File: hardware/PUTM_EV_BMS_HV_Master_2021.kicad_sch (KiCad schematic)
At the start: 22 parts, among them SW1 RESET, U19 STM32F446RETx, Y1 20MHz, Y2 32.768kHz

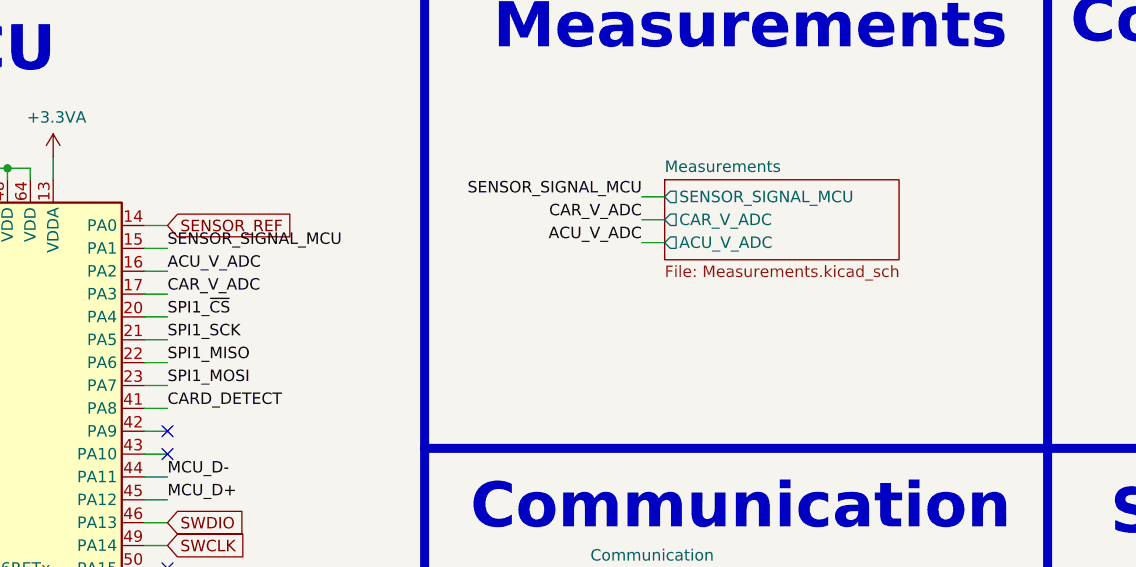
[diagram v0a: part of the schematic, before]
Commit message: changed HV measurements from isolated opamp to isolated ADC with isolated spi communication, changed safety laatching from mosfet back to relay
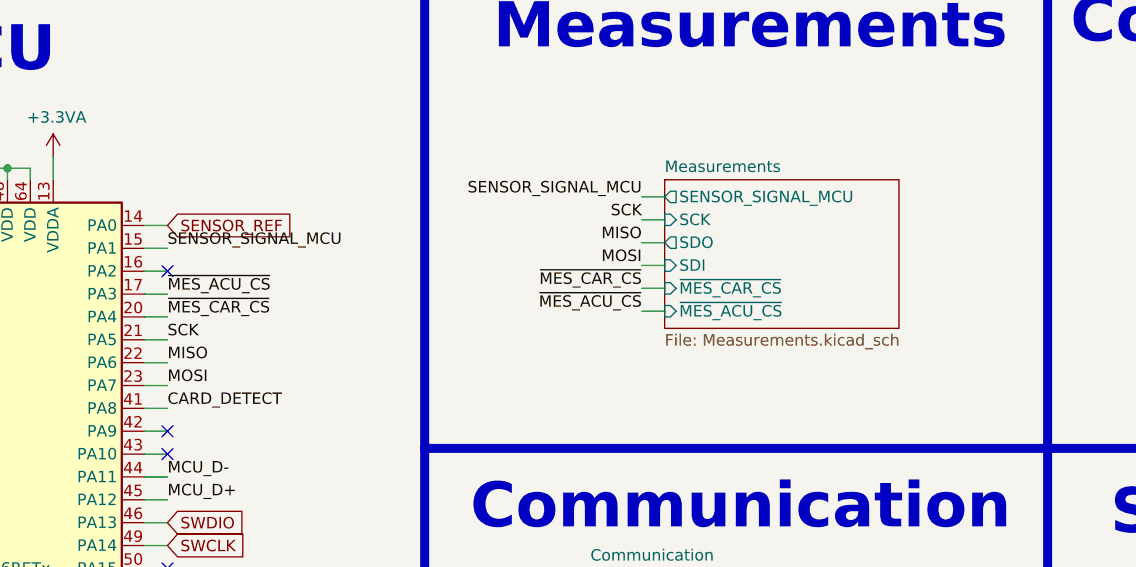
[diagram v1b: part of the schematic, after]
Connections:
- net SPI1_MISO: no longer U19.22 (PA6)
- net SPI1_MOSI: no longer U19.23 (PA7)
- net SPI1_SCK: no longer U19.21 (PA5)
- net SPI1_~{CS}: no longer U19.20 (PA4)
- net ACU_V_ADC: no longer names the net of U19.16 (PA2)
- net CAR_V_ADC renamed ~{MES_ACU_CS}
- new net MISO: U19.22 (PA6)
- new net MOSI: U19.23 (PA7)
- new net SCK: U19.21 (PA5)
- new net ~{MES_CAR_CS}: U19.20 (PA4)
- no-connect marks 9 -> 10
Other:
- sheet Measurements ports: added SCK, SDI, SDO, ~{MES_ACU_CS}, ~{MES_CAR_CS}; removed ACU_V_ADC, CAR_V_ADC

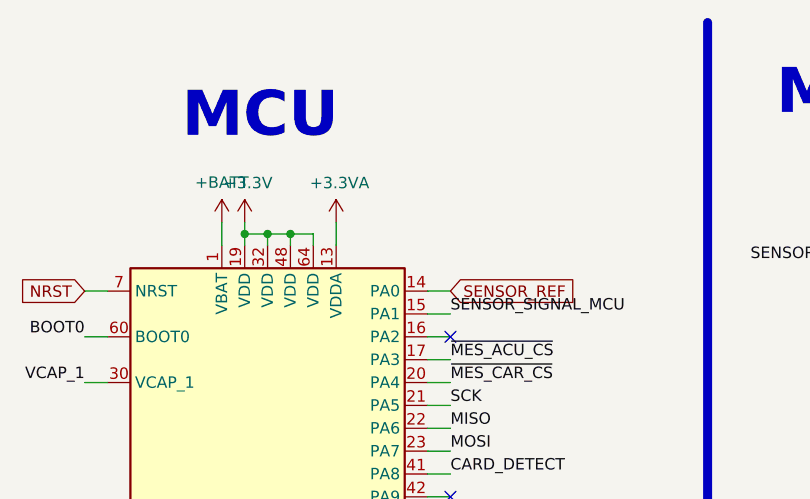
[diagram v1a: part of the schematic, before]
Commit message: changed the 1V voltage ref made from RL circuit to low noise, 0.1% error 1.024 V ref gen, and changed the opamp used for current sensor feedback filtration to a high precision low drift opamp
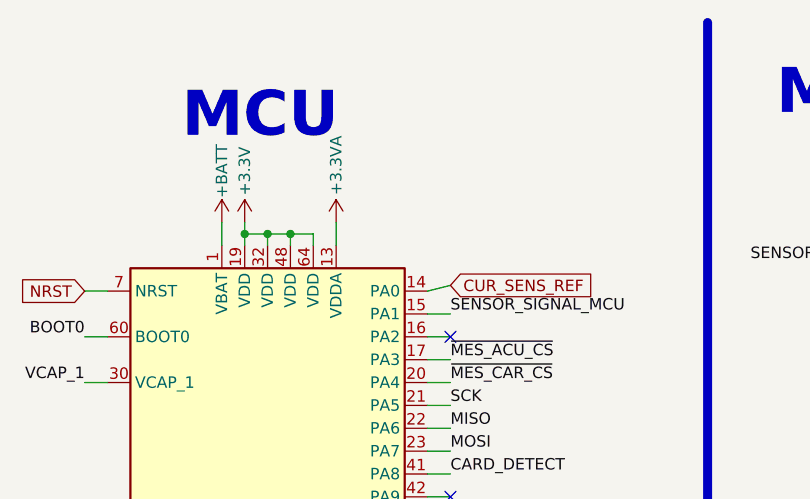
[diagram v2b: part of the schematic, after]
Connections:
- net SENSOR_REF renamed CUR_SENS_REF

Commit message: pcb update
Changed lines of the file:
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@@
     (stroke (width 0) (type default) (color 0 0 0 0))
   )
-  (wire (pts (xy 78.74 41.275) (xy 76.2 41.91))
+  (wire (pts (xy 78.74 41.91) (xy 76.2 41.91))
     (stroke (width 0) (type default) (color 0 0 0 0))
   )
@@
   )
   (wire (pts (xy 245.11 152.4) (xy 246.38 152.4))
+    (stroke (width 0) (type default) (color 0 0 0 0))
+  )
+  (wire (pts (xy 78.74 39.37) (xy 78.74 41.91))
     (stroke (width 0) (type default) (color 0 0 0 0))
   )
@@
     )
   )
-  (global_label "CUR_SENS_REF" (shape input) (at 78.74 41.275 0) (fields_autoplaced)
+  (global_label "CUR_SENS_REF" (shape input) (at 78.74 39.37 90) (fields_autoplaced)
     (effects (font (size 1.27 1.27)) (justify left))
-    (property "Intersheet References" "${INTERSHEET_REFS}" (id 0) (at 95.2761 41.1956 0)
+    (property "Intersheet References" "${INTERSHEET_REFS}" (id 0) (at 78.6606 22.8339 90)
       (effects (font (size 1.27 1.27)) (justify left) hide)
     )
@@
     (path "/6eb4a2b1-8e5b-451b-b593-8aaaa3a4213e/940d36fb-8f48-4fee-84f0-e5e0ba24df3f" (page "19"))
     (path "/81dc0685-0bdd-4dc2-8f76-92836044cf1e/b8954743-0175-4ee0-bad0-8f0716e13306" (page "21"))
+    (path "/6eb4a2b1-8e5b-451b-b593-8aaaa3a4213e/fd8c1b79-afed-4653-bb63-44888bf7ecb3" (page "23"))
     (path "/e61cc821-5479-4c04-b5ab-4a32f17b4f03" (page "23"))
-    (path "/6eb4a2b1-8e5b-451b-b593-8aaaa3a4213e/fd8c1b79-afed-4653-bb63-44888bf7ecb3" (page "23"))
     (path "/e61cc821-5479-4c04-b5ab-4a32f17b4f03/d2e30d51-b8f8-4bbd-bb5a-76e0eb119260" (page "24"))
     (path "/e61cc821-5479-4c04-b5ab-4a32f17b4f03/6b03d8c8-5f6c-4244-9202-23821031eb5e" (page "25"))
@@
       (reference "#PWR0181") (unit 1) (value "GND") (footprint "")
     )
+    (path "/e61cc821-5479-4c04-b5ab-4a32f17b4f03/4d685d28-82a8-4b66-8595-b56b352d024f"
+      (reference "#PWR0182") (unit 1) (value "+3.3V") (footprint "")
+    )
+    (path "/e61cc821-5479-4c04-b5ab-4a32f17b4f03/1ea820be-8637-4045-bb25-65f2e6b38534"
+      (reference "#PWR0183") (unit 1) (value "GND") (footprint "")
+    )
     (path "/6eb4a2b1-8e5b-451b-b593-8aaaa3a4213e/976a27c2-83d9-4e7e-aa84-83f0286fd11b"
       (reference "#PWR0192") (unit 1) (value "+5V") (footprint "")
     )
-    (path "/e61cc821-5479-4c04-b5ab-4a32f17b4f03/1ea820be-8637-4045-bb25-65f2e6b38534"
-      (reference "#PWR?") (unit 1) (value "GND") (footprint "")
-    )
-    (path "/e61cc821-5479-4c04-b5ab-4a32f17b4f03/4d685d28-82a8-4b66-8595-b56b352d024f"
-      (reference "#PWR?") (unit 1) (value "+3.3V") (footprint "")
-    )
     (path "/66c3869d-de11-4d8d-b4de-9d98c32ec205/ddeb9dfe-eb2d-4bf5-bf14-a97849901813"
       (reference "BT1") (unit 1) (value "KEYSTONE 103") (footprint "Battery:BatteryHolder_Keystone_103_1x20mm")
@@
     )
     (path "/e61cc821-5479-4c04-b5ab-4a32f17b4f03/0ed0fccf-7332-4a4b-a5be-653ad796ee03"
-      (reference "IC?") (unit 1) (value "ADA4505-1ARJZ-R7") (footprint "SOT95P280X145-5N")
+      (reference "IC6") (unit 1) (value "ADA4505-1ARJZ-R7") (footprint "SOT95P280X145-5N")
     )
     (path "/568caa85-d8c4-4885-aabf-c5422dff8b33/5d810376-fb11-4708-9087-e616d0e24c83"

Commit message: schemat sync
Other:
- sheet Measurements ports: added ~{SENS_CS}; removed none

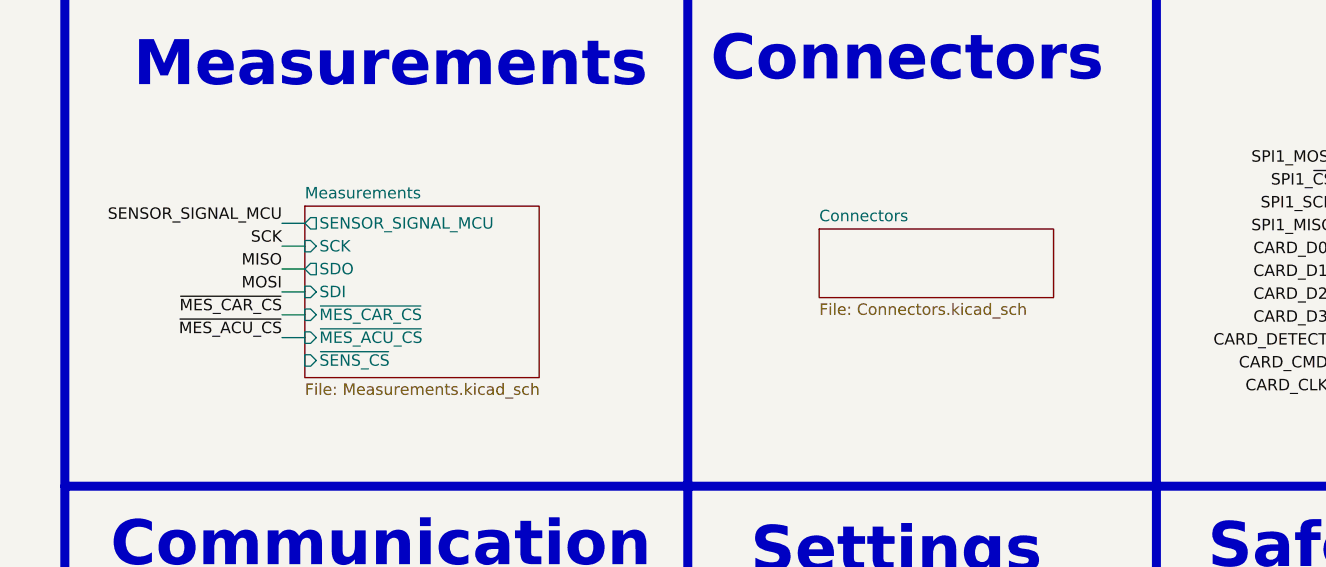
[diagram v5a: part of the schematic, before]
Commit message: measurments section changes, sorted components on the board into groups, changed main connector and added seprate for AIRs, added IMD PWM input as well as AIR fault detection
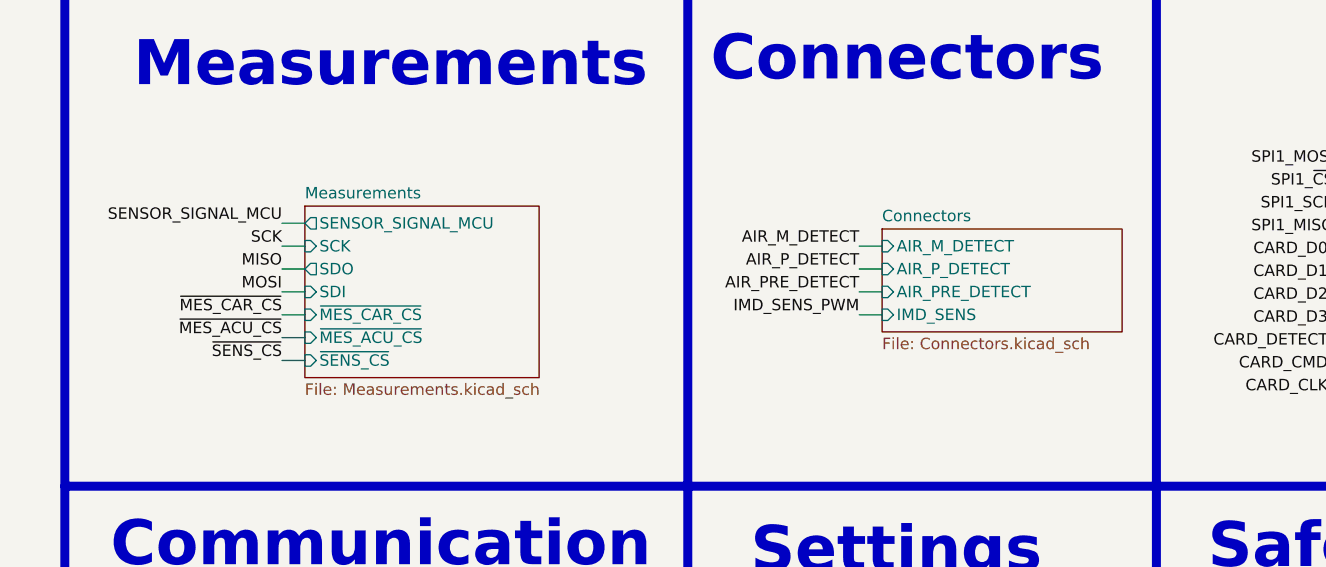
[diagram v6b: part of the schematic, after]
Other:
- sheet Connectors ports: added AIR_M_DETECT, AIR_PRE_DETECT, AIR_P_DETECT, IMD_SENS; removed none

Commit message: changed few connectors, finished board HV section and other minor changes
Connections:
- net AIR_M_DETECT: now also U19.59 (PB7)
- net AIR_PRE_DETECT: now also U19.57 (PB5)
- net AIR_P_DETECT: now also U19.58 (PB6)
- net DIN_1_MCU: now also U19.56 (PB4); no longer U19.57 (PB5)
- net DIN_2_MCU: now also U19.55 (PB3); no longer U19.56 (PB4)
- net DIN_3_MCU: now also U19.28 (PB2); no longer U19.55 (PB3)
- net IMD_SENS_PWM: now also U19.42 (PA9)
- net MCU_LED_1: now also U19.26 (PB0); no longer U19.27 (PB1)
- net MCU_LED_2: now also U19.27 (PB1); no longer U19.28 (PB2)
- net ~{SENS_CS}: now also U19.16 (PA2)
- net SENSOR_SIGNAL_MCU: no longer names the net of U19.15 (PA1)
- no-connect marks 10 -> 6
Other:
- sheet Measurements ports: added none; removed SENSOR_SIGNAL_MCU
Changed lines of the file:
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@@
   (no_connect (at 78.74 67.31))
   (no_connect (at 38.1 95.25))
+  (no_connect (at 78.74 44.45))
   (no_connect (at 78.74 80.01))
   (no_connect (at 38.1 115.57))
-  (no_connect (at 78.74 64.77))
-  (no_connect (at 78.74 100.33))
-  (no_connect (at 78.74 102.87))
-  (no_connect (at 78.74 46.99))
   (no_connect (at 78.74 113.03))
-  (no_connect (at 78.74 85.09))
   (wire (pts (xy 41.275 184.785) (xy 41.275 186.055))
     (stroke (width 0) (type default) (color 0 0 0 0))
@@
     (stroke (width 0) (type default) (color 0 0 0 0))
   )
-  (wire (pts (xy 131.445 37.465) (xy 133.985 37.465))
-    (stroke (width 0) (type default) (color 0 0 0 0))
-  )
   (wire (pts (xy 197.485 95.885) (xy 194.945 95.885))
     (stroke (width 0) (type default) (color 0 0 0 0))
@@
     (effects (font (size 1.27 1.27)) (justify right bottom))
   )
-  (label "NRST" (at 123.19 112.395 180)
-    (effects (font (size 1.27 1.27)) (justify right bottom))
-  )
   (label "PHASE" (at 159.385 86.995 0)
     (effects (font (size 1.27 1.27)) (justify left bottom))
@@
     (effects (font (size 1.27 1.27)) (justify right bottom))
   )
-  (label "SENSOR_SIGNAL_MCU" (at 131.445 37.465 180)
-    (effects (font (size 1.27 1.27)) (justify right bottom))
-  )
   (label "CARD_DETECT" (at 247.65 51.435 180)
     (effects (font (size 1.27 1.27)) (justify right bottom))
@@
     (effects (font (size 1.27 1.27)) (justify right bottom))
   )
-  (label "DIN_1_MCU" (at 78.74 97.79 0)
+  (label "DIN_1_MCU" (at 78.74 95.25 0)
     (effects (font (size 1.27 1.27)) (justify left bottom))
   )
@@
     (effects (font (size 1.27 1.27)) (justify right bottom))
   )
-  (label "MCU_LED_1" (at 78.74 87.63 0)
+  (label "MCU_LED_1" (at 78.74 85.09 0)
     (effects (font (size 1.27 1.27)) (justify left bottom))
   )
@@
     (effects (font (size 1.27 1.27)) (justify right bottom))
   )
+  (label "AIR_PRE_DETECT" (at 78.74 97.79 0)
+    (effects (font (size 1.27 1.27)) (justify left bottom))
+  )
   (label "MASTER_MODE" (at 159.385 84.455 0)
     (effects (font (size 1.27 1.27)) (justify left bottom))
@@
     (effects (font (size 1.27 1.27)) (justify right bottom))
   )
-  (label "DIN_3_MCU" (at 78.74 92.71 0)
+  (label "DIN_3_MCU" (at 78.74 90.17 0)
     (effects (font (size 1.27 1.27)) (justify left bottom))
   )
@@
     (effects (font (size 1.27 1.27)) (justify right bottom))
   )
-  (label "SENSOR_SIGNAL_MCU" (at 78.74 44.45 0)
-    (effects (font (size 1.27 1.27)) (justify left bottom))
-  )
   (label "SPI1_SCK" (at 248.285 36.195 180)
     (effects (font (size 1.27 1.27)) (justify right bottom))
@@
     (effects (font (size 1.27 1.27)) (justify right bottom))
   )
+  (label "AIR_P_DETECT" (at 78.74 100.33 0)
+    (effects (font (size 1.27 1.27)) (justify left bottom))
+  )
   (label "RTC_CLK_OUT" (at 255.27 152.4 0)
     (effects (font (size 1.27 1.27)) (justify left bottom))
@@
     (effects (font (size 1.27 1.27)) (justify right bottom))
   )
+  (label "AIR_M_DETECT" (at 78.74 102.87 0)
+    (effects (font (size 1.27 1.27)) (justify left bottom))
+  )
   (label "RTC_CLK_OUT" (at 38.1 120.65 180)
     (effects (font (size 1.27 1.27)) (justify right bottom))
@@
     (effects (font (size 1.27 1.27)) (justify right bottom))
   )
+  (label "~{SENS_CS}" (at 78.74 46.99 0)
+    (effects (font (size 1.27 1.27)) (justify left bottom))
+  )
   (label "AMS_FAULT_MCU" (at 38.1 92.71 180)
     (effects (font (size 1.27 1.27)) (justify right bottom))
@@
     (effects (font (size 1.27 1.27)) (justify right bottom))
   )
-  (label "MCU_LED_2" (at 78.74 90.17 0)
+  (label "MCU_LED_2" (at 78.74 87.63 0)
     (effects (font (size 1.27 1.27)) (justify left bottom))
   )
@@
     (effects (font (size 1.27 1.27)) (justify right bottom))
   )
+  (label "IMD_SENS_PWM" (at 78.74 64.77 0)
+    (effects (font (size 1.27 1.27)) (justify left bottom))
+  )
   (label "CARD_CLK" (at 247.65 56.515 180)
     (effects (font (size 1.27 1.27)) (justify right bottom))
@@
     (effects (font (size 1.27 1.27)) (justify right bottom))
   )
-  (label "DIN_2_MCU" (at 78.74 95.25 0)
+  (label "DIN_2_MCU" (at 78.74 92.71 0)
     (effects (font (size 1.27 1.27)) (justify left bottom))
   )
@@
     (property "Intersheet References" "${INTERSHEET_REFS}" (id 0) (at 189.3468 141.5256 0)
       (effects (font (size 1.27 1.27)) (justify left) hide)
+    )
+  )
+  (global_label "NRST" (shape input) (at 123.19 112.395 180) (fields_autoplaced)
+    (effects (font (size 1.27 1.27)) (justify right))
+    (property "Intersheet References" "${INTERSHEET_REFS}" (id 0) (at 116.0882 112.4744 0)
+      (effects (font (size 1.27 1.27)) (justify right) hide)
     )
   )
@@
     )
   )
-  (sheet (at 133.985 35.56) (size 26.035 19.05) (fields_autoplaced)
+  (sheet (at 133.985 38.1) (size 26.035 16.51) (fields_autoplaced)
     (stroke (width 0.1524) (type solid) (color 0 0 0 0))
     (fill (color 0 0 0 0.0000))
-    (property "Sheet name" "Measurements" (id 0) (at 133.985 34.8484 0)
+    (property "Sheet name" "Measurements" (id 0) (at 133.985 37.3884 0)
       (effects (font (size 1.27 1.27)) (justify left bottom))
     )
     (property "Sheet file" "Measurements.kicad_sch" (id 1) (at 133.985 55.1946 0)
       (effects (font (size 1.27 1.27)) (justify left top))
-    )
-    (pin "SENSOR_SIGNAL_MCU" output (at 133.985 37.465 180)
-      (effects (font (size 1.27 1.27)) (justify left))
     )
     (pin "SCK" input (at 133.985 40.005 180)
@@
       (reference "#PWR0127") (unit 1) (value "GND") (footprint "")
     )
-    (path "/568caa85-d8c4-4885-aabf-c5422dff8b33/ef8254a5-dbc4-4491-aadd-96c0379e49a2"
-      (reference "#PWR0128") (unit 1) (value "USB_GND") (footprint "")
-    )
     (path "/6eb4a2b1-8e5b-451b-b593-8aaaa3a4213e/5bd9a2ee-5407-466e-aec2-5c41610e892b"
       (reference "#PWR0129") (unit 1) (value "GND") (footprint "")
@@
       (reference "J1") (unit 1) (value "USB_C_Receptacle_USB2.0") (footprint "Connector_USB:USB_C_Receptacle_HRO_TYPE-C-31-M-12")
     )
-    (path "/568caa85-d8c4-4885-aabf-c5422dff8b33/875e42a9-ac49-4cd8-8bf1-12b7b778e16e"
-      (reference "J2") (unit 1) (value "M80-5012622") (footprint "M80-50126YY")
+    (path "/568caa85-d8c4-4885-aabf-c5422dff8b33/f4e1e24b-a2bf-45dc-a4a4-8f6fafdff401"
+      (reference "J2") (unit 1) (value "M80-5302642") (footprint "M80-53026YY")
     )
     (path "/568caa85-d8c4-4885-aabf-c5422dff8b33/cd5cf272-3ba3-46b1-9c96-dbbc87134393"
       (reference "J3") (unit 1) (value "M300-MV31045M1") (footprint "M300MV31045M1")
     )
-    (path "/568caa85-d8c4-4885-aabf-c5422dff8b33/1c34780a-54a9-4e53-89dc-1382efaf435e"
-      (reference "J4") (unit 1) (value "Harw_Conn_1x2") (footprint "M808420245")
-    )
-    (path "/568caa85-d8c4-4885-aabf-c5422dff8b33/95bc52eb-dd6c-4947-888e-17e975ed0a12"
-      (reference "J5") (unit 1) (value "Harw_Conn_1x2") (footprint "M808420245")
-    )
-    (path "/568caa85-d8c4-4885-aabf-c5422dff8b33/5fc028c5-2f7a-4d94-92ab-d8ae123d6f9c"
-      (reference "J6") (unit 1) (value "Harw_Conn_1x4") (footprint "M80-8420445")
+    (path "/568caa85-d8c4-4885-aabf-c5422dff8b33/9282f25c-4541-4ee9-bd8c-e697fdd3ec49"
+      (reference "J4") (unit 1) (value "M80-5L10442MC") (footprint "M80-5L104YYMC")
+    )
+    (path "/568caa85-d8c4-4885-aabf-c5422dff8b33/a2f87785-705e-47f0-84ef-eeb990e33238"
+      (reference "J5") (unit 1) (value "M80-5L10442MC") (footprint "M80-5L104YYMC")
+    )
+    (path "/568caa85-d8c4-4885-aabf-c5422dff8b33/112611ea-4877-4f1d-a788-f9d939bbc0d0"
+      (reference "J6") (unit 1) (value "M80-5L10442MC") (footprint "M80-5L104YYMC")
     )
     (path "/568caa85-d8c4-4885-aabf-c5422dff8b33/38c113a9-0789-443f-88b4-8b25cffca385"
